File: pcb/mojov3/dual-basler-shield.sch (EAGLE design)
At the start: 19 parts

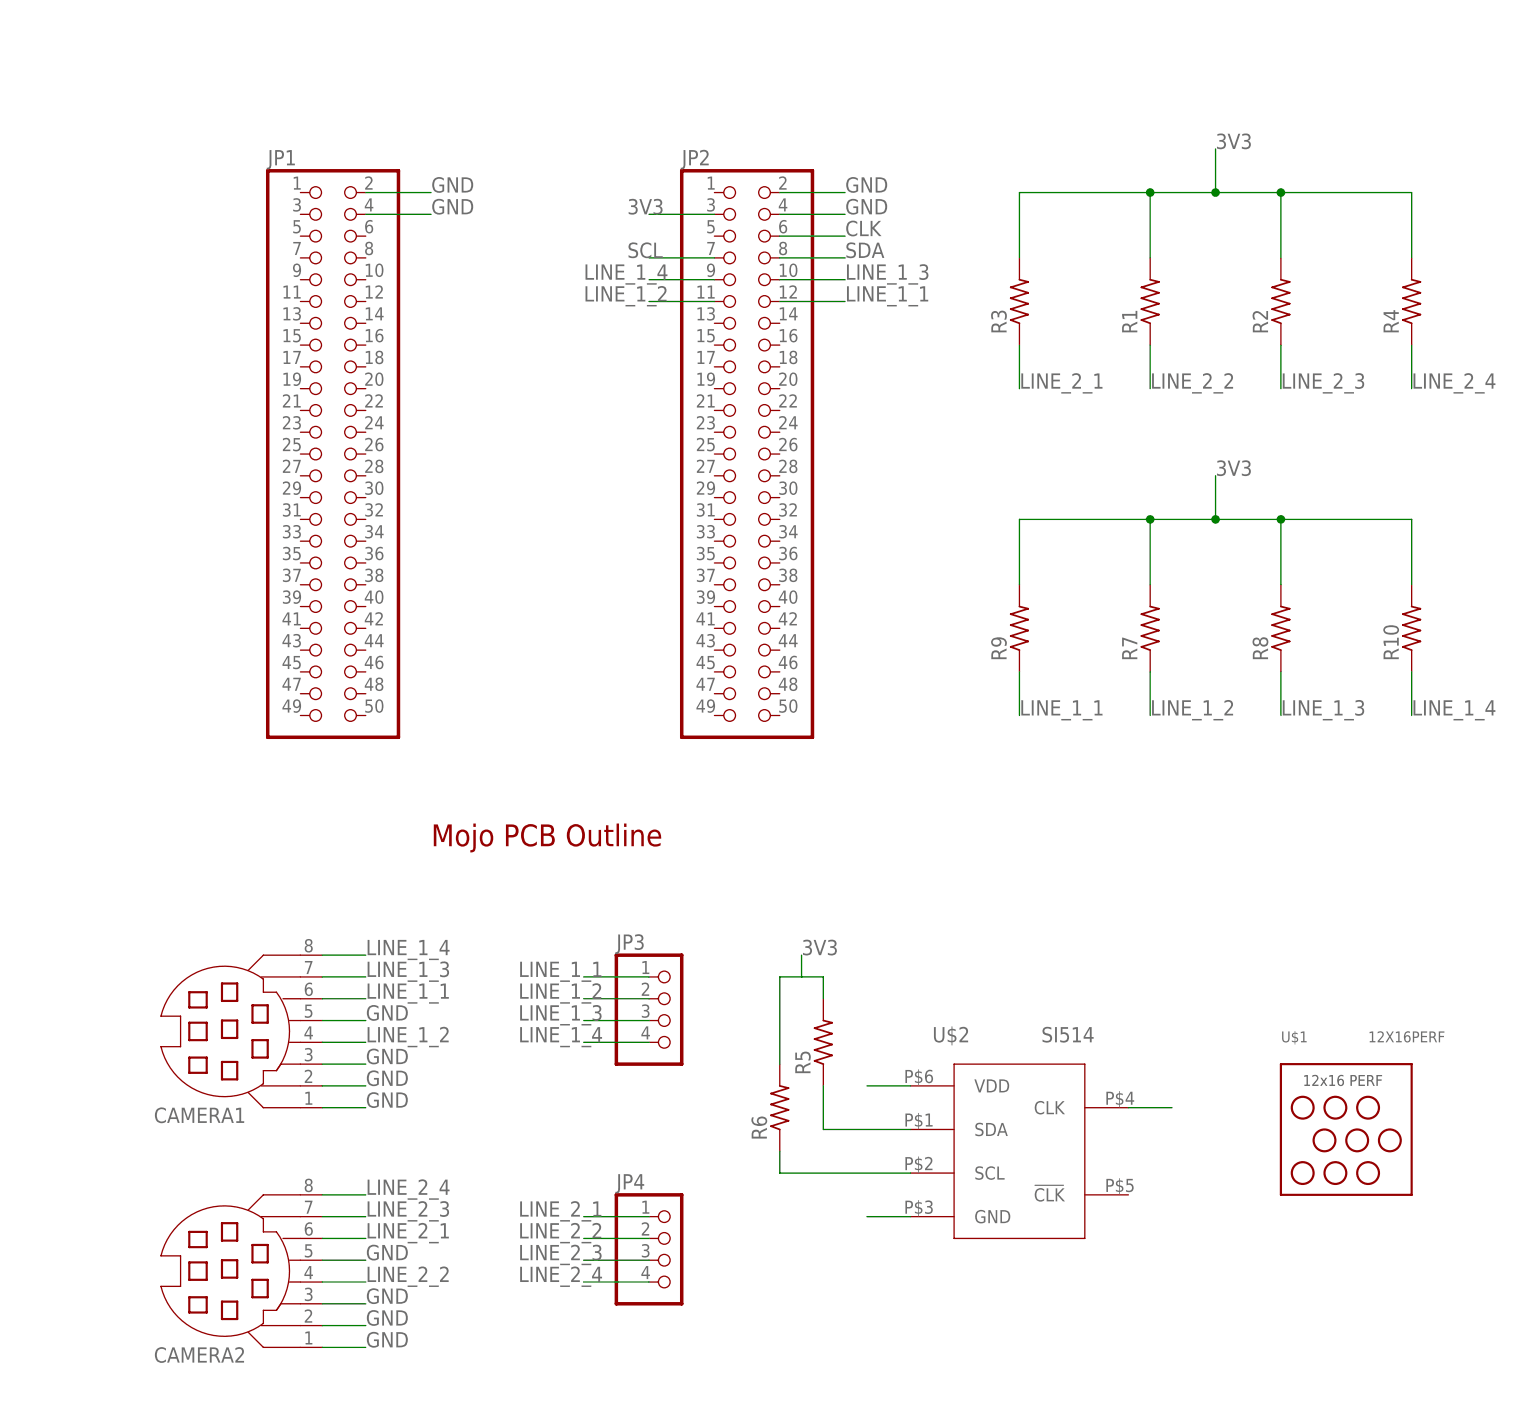
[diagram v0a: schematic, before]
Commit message: dual basler shield circuit complete
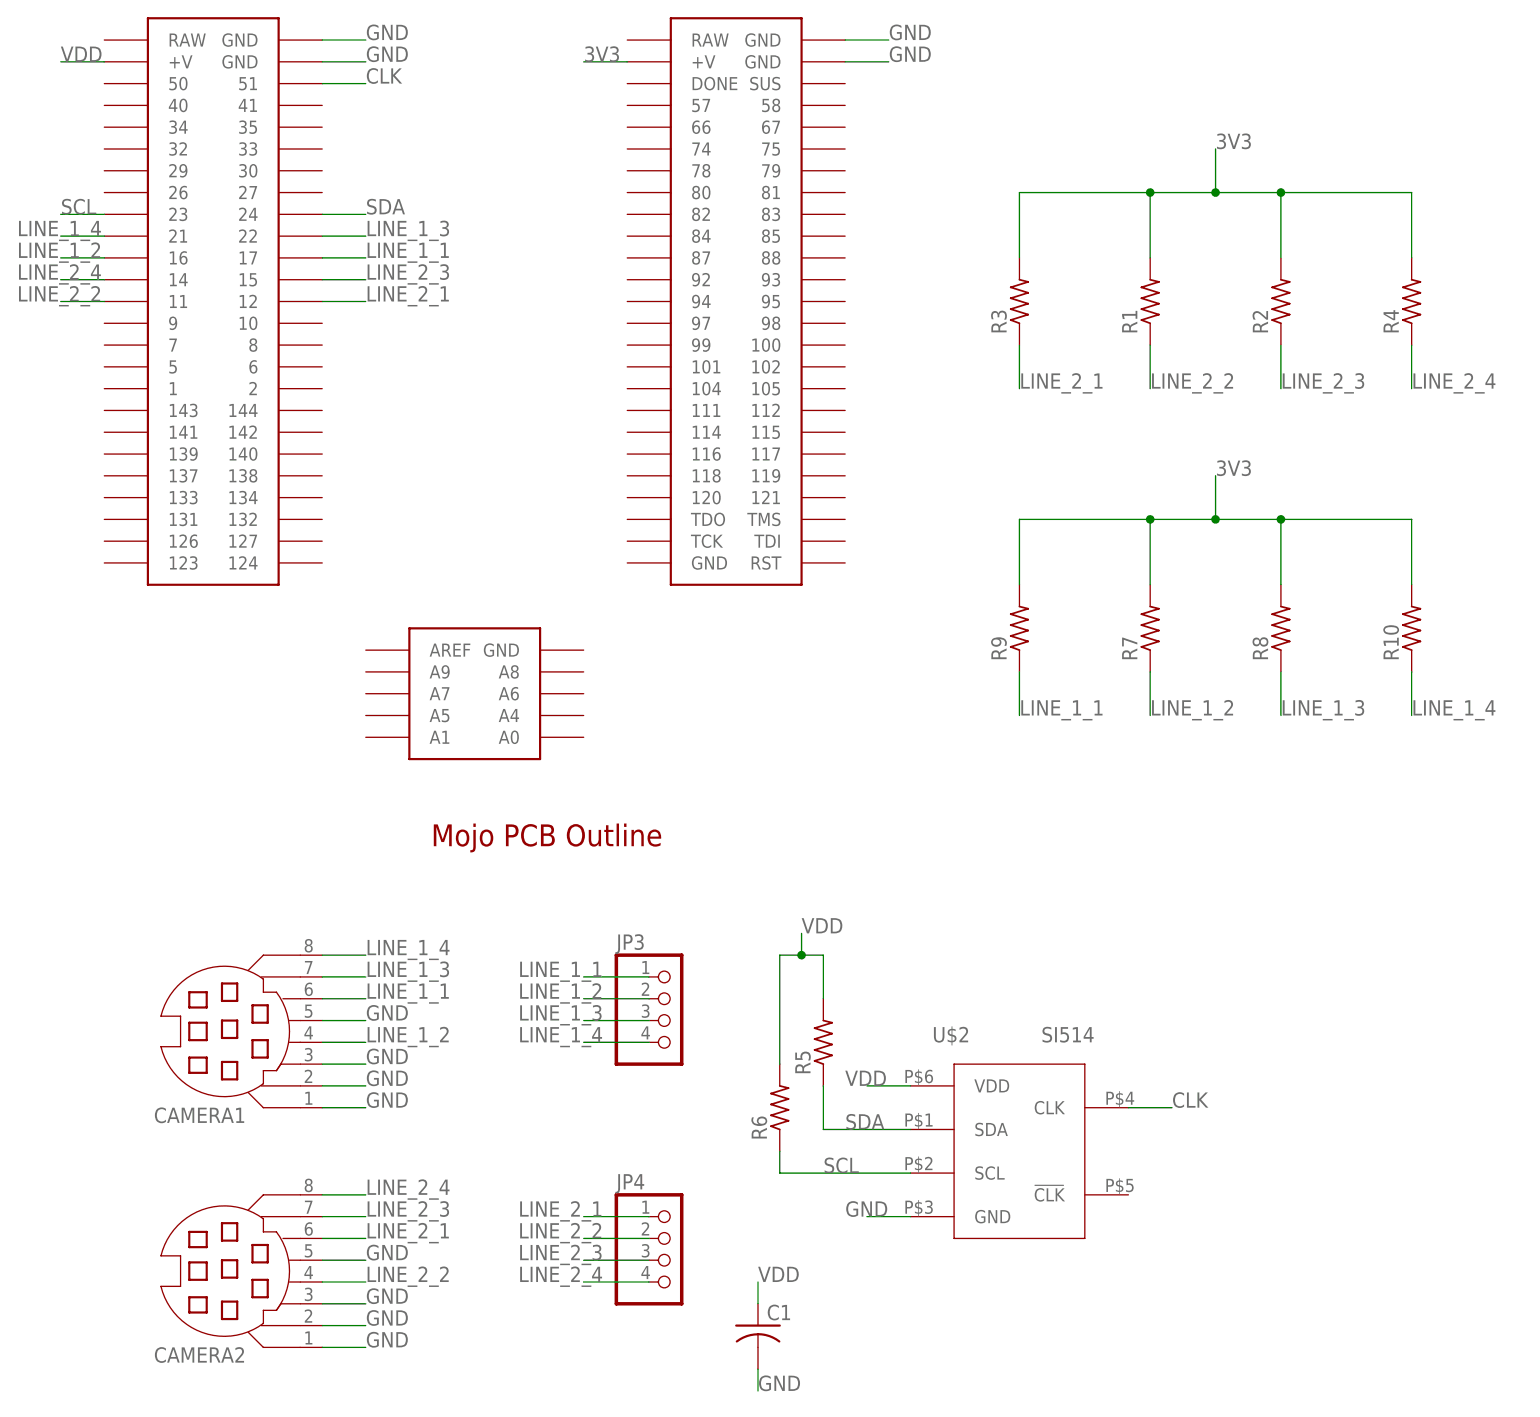
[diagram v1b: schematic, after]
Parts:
- removed JP1, JP2: (no value), pinhead:PINHD-2X25
- removed U$1: 12X16PERF, custom-regs:12X16PERF
- added C1: (no value), rcl:C-USC0603
- added U$4: MOJOV3, EmbeddedMicro-Mojo:MOJOV3
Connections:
- removed net GND1: U$2.GND
- new net VDD: C1.1, R5.2, R6.2, U$2.VDD, U$4G$2.+V
- net 3V3: now also U$4G$3.+V; no longer JP2.3, R5.2, R6.2, U$2.VDD
- net CLK: now also U$4G$2.51; no longer JP2.6
- net GND: now also C1.2, U$2.GND, U$4G$2.GND@1, U$4G$2.GND@2, U$4G$3.GND@1, U$4G$3.GND@2; no longer JP1.2, JP1.4, JP2.2, JP2.4
- net LINE_1_1: now also U$4G$2.17; no longer JP2.12
- net LINE_1_2: now also U$4G$2.16; no longer JP2.11
- net LINE_1_3: now also U$4G$2.22; no longer JP2.10
- net LINE_1_4: now also U$4G$2.21; no longer JP2.9
- net LINE_2_1: now also U$4G$2.12
- net LINE_2_2: now also U$4G$2.11
- net LINE_2_3: now also U$4G$2.15
- net LINE_2_4: now also U$4G$2.14
- net SCL: now also U$4G$2.23; no longer JP2.7
- net SDA: now also U$4G$2.24; no longer JP2.8

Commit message: dual basler shield silkscreen edit
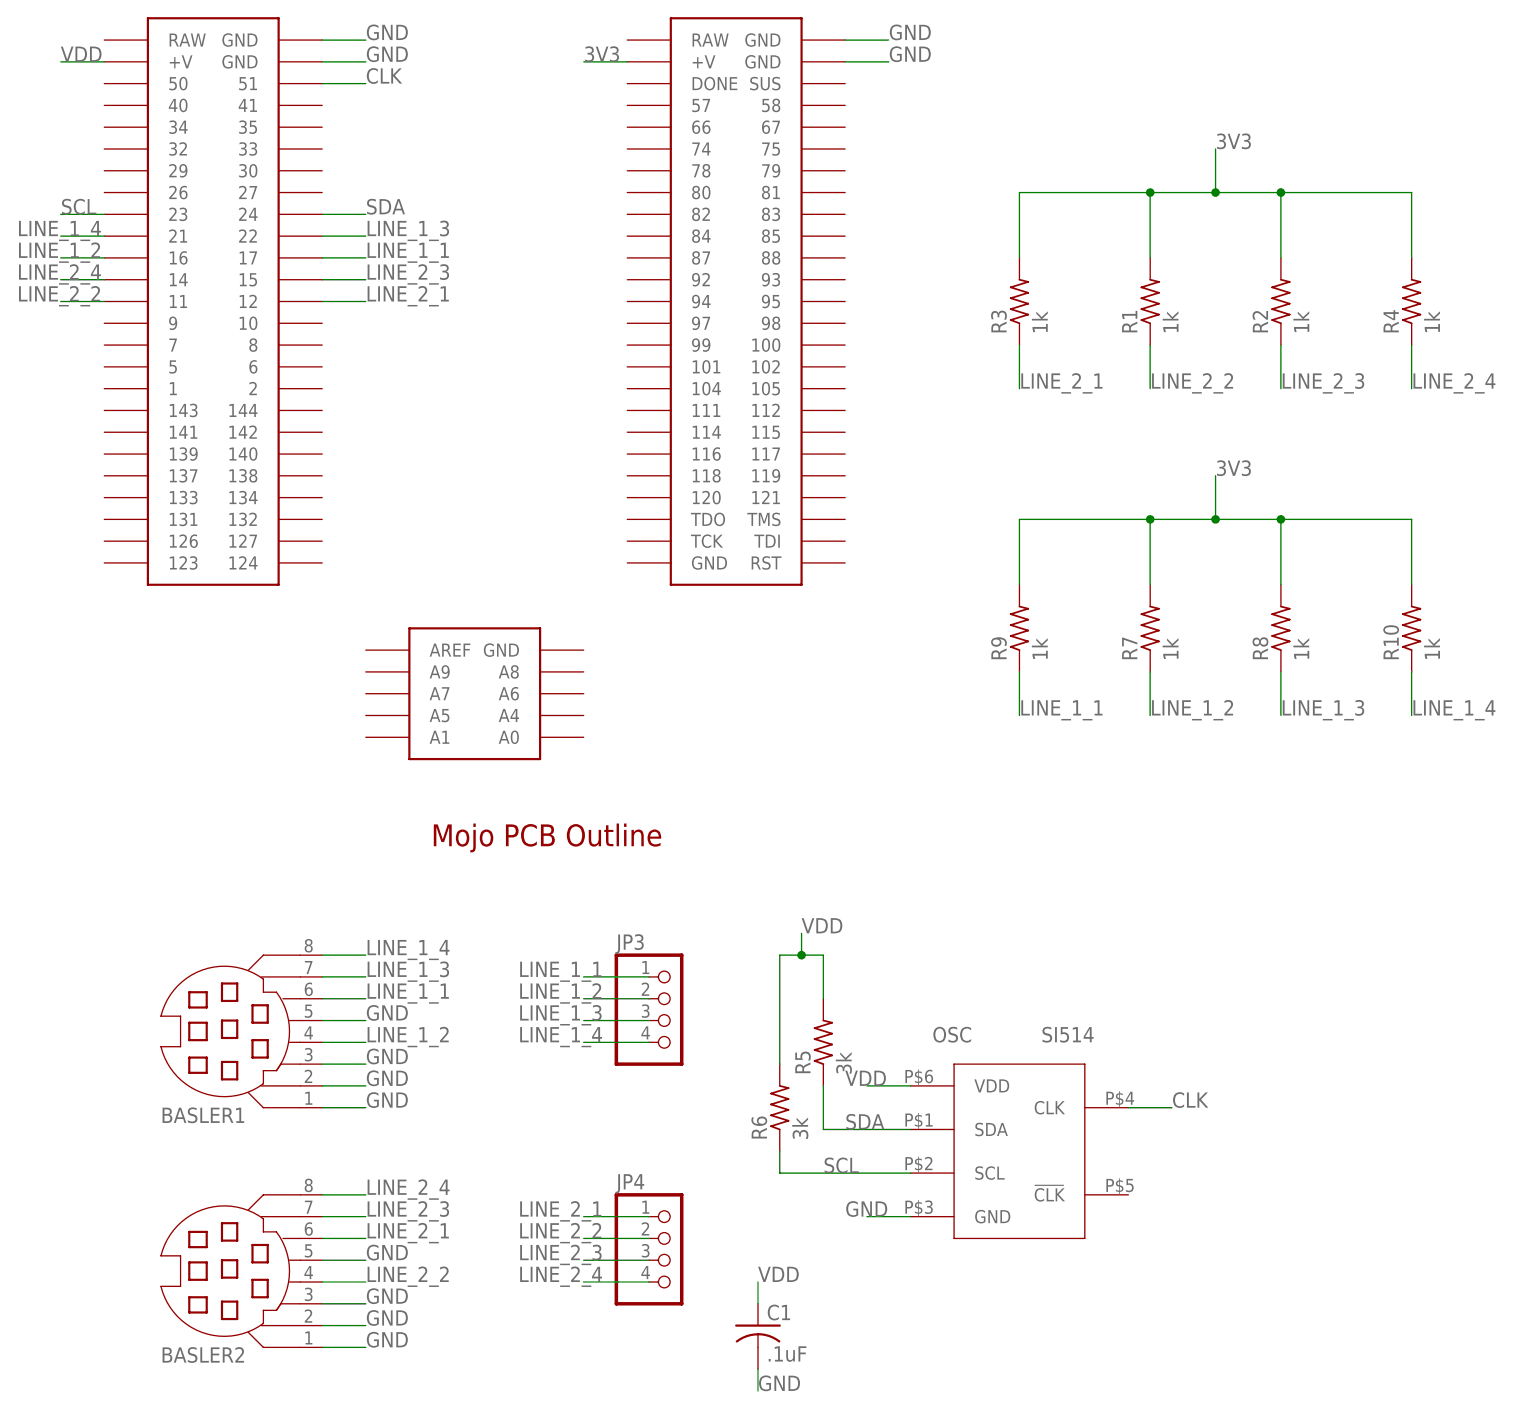
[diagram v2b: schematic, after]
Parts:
- C1: value (none) -> .1uF
- R1, R10, R2, R3, R4, R7, R8, R9: value (none) -> 1k
- R5, R6: value (none) -> 3k
- renumbered CAMERA1 to BASLER1, CAMERA2 to BASLER2, U$2 to OSC
